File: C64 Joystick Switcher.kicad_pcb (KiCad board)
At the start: 2 copper layers, 49.3 x 81.9 mm, 30 parts, among them J1 Port 1, J2 Port 2, J3 Joystick, J4 B2_SEL, J5 B1_SEL, Q1 BC547, SW1 P1_SEL, SW2 P2_SEL, U1 74HCT4053, U2 74HCT4053, U3 NE555, U4 NE555

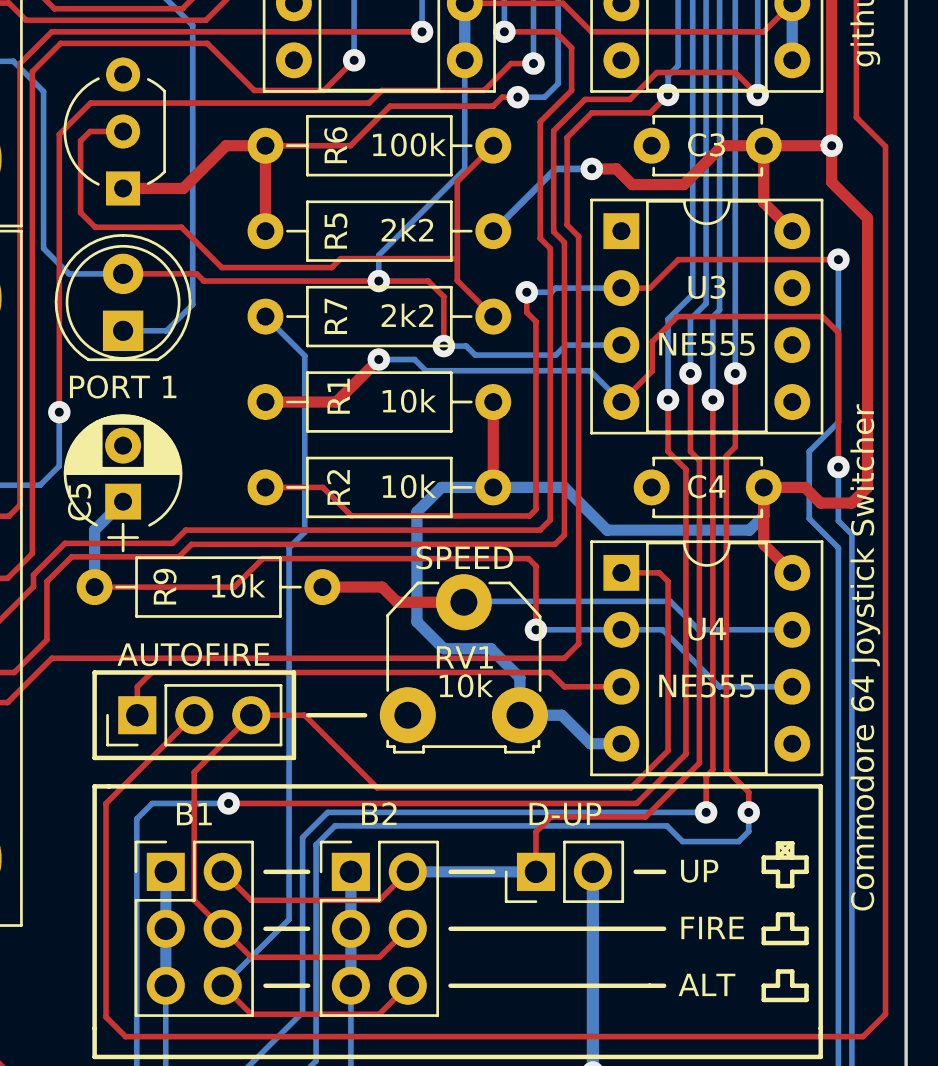
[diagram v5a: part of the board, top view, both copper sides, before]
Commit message: More small layout improvements
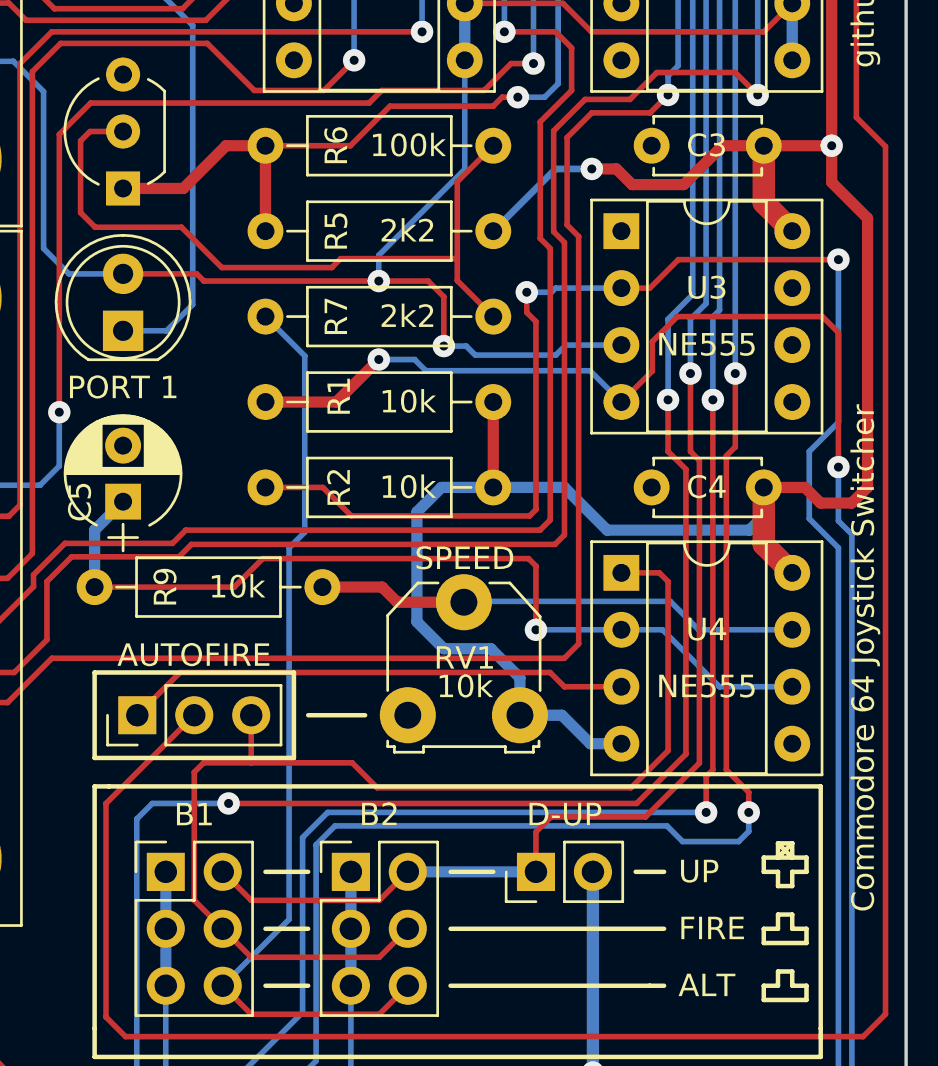
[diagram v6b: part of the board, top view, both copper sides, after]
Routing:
- net AUTOFIRE: track 23.4 -> 22.6 mm
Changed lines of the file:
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@@
     (thickness 1.6)
     (drawings 104)
-    (tracks 509)
+    (tracks 510)
     (zones 0)
     (modules 30)
@@
       (plotinvisibletext false)
       (padsonsilk false)
-      (subtractmaskfromsilk false)
+      (subtractmaskfromsilk true)
       (outputformat 1)
       (mirror false)
@@
   (segment (start 133.985 80.01) (end 140.335 80.01) (width 0.5) (layer B.Cu) (net 4))
   (segment (start 100.7 83.545) (end 100.7 102) (width 0.5) (layer F.Cu) (net 4))
-  (segment (start 140.97 80.645) (end 142.24 81.915) (width 0.5) (layer F.Cu) (net 4))
-  (segment (start 140.97 78.105) (end 140.97 80.645) (width 0.5) (layer F.Cu) (net 4))
+  (segment (start 140.97 80.645) (end 142.24 81.915) (width 1) (layer F.Cu) (net 4))
+  (segment (start 140.97 78.105) (end 140.97 80.645) (width 1) (layer F.Cu) (net 4))
   (via (at 144 62.865) (size 1) (drill 0.4) (layers F.Cu B.Cu) (net 4))
   (segment (start 131.68 63.9) (end 128.905 66.675) (width 0.3) (layer B.Cu) (net 4))
@@
   (segment (start 134.4 63.9) (end 135.1 64.6) (width 0.5) (layer F.Cu) (net 4))
   (segment (start 133.3 63.9) (end 134.4 63.9) (width 0.5) (layer F.Cu) (net 4))
-  (segment (start 140.97 65.405) (end 142.24 66.675) (width 0.5) (layer F.Cu) (net 4))
-  (segment (start 140.97 62.865) (end 140.97 65.405) (width 0.5) (layer F.Cu) (net 4))
+  (segment (start 140.97 65.405) (end 142.24 66.675) (width 1) (layer F.Cu) (net 4))
+  (segment (start 140.97 62.865) (end 140.97 65.405) (width 1) (layer F.Cu) (net 4))
   (segment (start 128.905 74.295) (end 128.905 78.105) (width 0.5) (layer F.Cu) (net 4))
   (segment (start 132.08 78.105) (end 128.905 78.105) (width 0.5) (layer B.Cu) (net 4))
@@
   (segment (start 123.825 99.06) (end 125.095 97.79) (width 0.25) (layer F.Cu) (net 10))
   (segment (start 118.11 99.06) (end 123.825 99.06) (width 0.25) (layer F.Cu) (net 10))
-  (segment (start 115.57 90.805) (end 118.11 88.265) (width 0.25) (layer F.Cu) (net 10))
-  (segment (start 115.57 96.52) (end 115.57 90.805) (width 0.25) (layer F.Cu) (net 10))
-  (segment (start 116.84 97.79) (end 115.57 96.52) (width 0.25) (layer F.Cu) (net 10))
-  (segment (start 136.315 81.915) (end 134.62 81.915) (width 0.25) (layer F.Cu) (net 10))
-  (segment (start 136.7 82.3) (end 136.315 81.915) (width 0.25) (layer F.Cu) (net 10))
-  (segment (start 136.7 89.85) (end 136.7 82.3) (width 0.25) (layer F.Cu) (net 10))
-  (segment (start 135.05 91.5) (end 136.7 89.85) (width 0.25) (layer F.Cu) (net 10))
-  (segment (start 123.725 91.5) (end 135.05 91.5) (width 0.25) (layer F.Cu) (net 10))
-  (segment (start 120.49 88.265) (end 123.725 91.5) (width 0.25) (layer F.Cu) (net 10))
-  (segment (start 118.11 88.265) (end 120.49 88.265) (width 0.25) (layer F.Cu) (net 10))
+  (segment (start 115.57 96.52) (end 116.84 97.79) (width 0.25) (layer F.Cu) (net 10))
+  (segment (start 123.725 91.5) (end 122.6125 90.3875) (width 0.25) (layer F.Cu) (net 10))
+  (segment (start 135.05 91.5) (end 123.725 91.5) (width 0.25) (layer F.Cu) (net 10))
+  (segment (start 136.7 89.85) (end 135.05 91.5) (width 0.25) (layer F.Cu) (net 10))
+  (segment (start 136.7 82.3) (end 136.7 89.85) (width 0.25) (layer F.Cu) (net 10))
+  (segment (start 115.57 90.805) (end 115.57 96.52) (width 0.25) (layer F.Cu) (net 10))
+  (segment (start 136.315 81.915) (end 136.7 82.3) (width 0.25) (layer F.Cu) (net 10))
+  (segment (start 115.9875 90.3875) (end 115.57 90.805) (width 0.25) (layer F.Cu) (net 10))
+  (segment (start 134.62 81.915) (end 136.315 81.915) (width 0.25) (layer F.Cu) (net 10))
+  (segment (start 118.11 88.265) (end 118.11 90.3875) (width 0.25) (layer F.Cu) (net 10))
+  (segment (start 122.6125 90.3875) (end 118.11 90.3875) (width 0.25) (layer F.Cu) (net 10))
+  (segment (start 118.11 90.3875) (end 115.9875 90.3875) (width 0.25) (layer F.Cu) (net 10))
   (via (at 131.6 46.355) (size 1) (drill 0.4) (layers F.Cu B.Cu) (net 11))
   (via (at 109.55 74.75) (size 1) (drill 0.4) (layers F.Cu B.Cu) (net 11))
@@
   (segment (start 132.08 86.995) (end 134.62 86.995) (width 0.25) (layer F.Cu) (net 31))
   (segment (start 131.445 86.36) (end 132.08 86.995) (width 0.25) (layer F.Cu) (net 31))
-  (segment (start 113.665 86.36) (end 131.445 86.36) (width 0.25) (layer F.Cu) (net 31))
-  (segment (start 113.03 86.995) (end 113.665 86.36) (width 0.25) (layer F.Cu) (net 31))
-  (segment (start 113.03 88.265) (end 113.03 86.995) (width 0.25) (layer F.Cu) (net 31))
+  (segment (start 114.935 86.36) (end 113.03 88.265) (width 0.25) (layer F.Cu) (net 31))
+  (segment (start 131.445 86.36) (end 114.935 86.36) (width 0.25) (layer F.Cu) (net 31))
   (via (at 130.81 84.455) (size 1) (drill 0.4) (layers F.Cu B.Cu) (net 32))
   (segment (start 134.62 84.455) (end 130.81 84.455) (width 0.25) (layer B.Cu) (net 32))
